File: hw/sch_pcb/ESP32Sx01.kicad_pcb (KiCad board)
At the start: 2 copper layers, 60.5 x 50.3 mm, 32 parts, among them J1 HEADER_1x03, J2 USBC_USB4105-GF-A, J3 HEADER_1x12, J4 HEADER_1x12, J5 HEADER_1x12, J6 HEADER_1x03, J7 HEADER_1x03, J8 HEADER_2x05, Q1 BC817-25, SW1 434133025816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

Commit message: Update of PCB design
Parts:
- removed J7: HEADER_1x03, Mlab_Pin_Headers:Straight_2x03
- added Y1: Crystal_Small, Mlab_XTAL:ABS07, B.Cu at (152.4, 104.7)
- SW1: moved to F.Cu
- moved C7 80.8 mm to (162.2, 87.4), turned to 90 degrees
- moved C4 73.3 mm to (154.0, 102.6)
- moved C5 69.4 mm to (150.5, 102.6), turned to 0 degrees
- moved R1 64.4 mm to (168.9, 119.6), turned to 0 degrees
- moved SW1 58.3 mm to (130.1, 92.8), turned to 90 degrees
- moved R2 58.2 mm to (160.0, 119.7)
- moved D1 42.7 mm to (166.9, 84.7), turned to -90 degrees
- moved J1 40.6 mm to (153.1, 117.2)
- moved J6 34.5 mm to (132.7, 117.2)
- moved C6 33.1 mm to (135.6, 88.1)
- moved R4 29.6 mm to (164.3, 87.4), turned to -90 degrees
- moved R6 18.4 mm to (127.7, 83.8), turned to -90 degrees
- moved R3 18.0 mm to (134.0, 86.1), turned to 0 degrees
- moved Q1 15.8 mm to (128.1, 87.8), turned to 0 degrees
- moved R5 14.2 mm to (131.8, 88.2)
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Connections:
- J4 pad 1: Net-(J4-Pad1) -> GND
- J4 pad 10: Net-(J4-Pad10) -> /GPIO17
- J4 pad 11: Net-(J4-Pad11) -> /GPIO18
- J4 pad 12: Net-(J4-Pad11) -> /GPIO18
- J4 pad 13: Net-(J4-Pad13) -> /GPIO21
- J4 pad 14: Net-(J4-Pad13) -> /GPIO21
- J4 pad 15: Net-(J4-Pad15) -> /GPIO47
- J4 pad 16: Net-(J4-Pad15) -> /GPIO47
- J4 pad 17: Net-(J4-Pad17) -> /GPIO48
- J4 pad 18: Net-(J4-Pad17) -> /GPIO48
- J4 pad 19: Net-(J4-Pad19) -> GND
- J4 pad 2: Net-(J4-Pad1) -> GND
- J4 pad 20: Net-(J4-Pad19) -> GND
- J4 pad 21: Net-(J4-Pad21) -> +3V3
- J4 pad 22: Net-(J4-Pad21) -> +3V3
- J4 pad 23: Net-(J4-Pad23) -> GND
- J4 pad 24: Net-(J4-Pad23) -> GND
- J4 pad 3: Net-(J4-Pad3) -> /GPIO12
- J4 pad 4: Net-(J4-Pad3) -> /GPIO12
- J4 pad 5: Net-(J4-Pad5) -> /GPIO13
- J4 pad 6: Net-(J4-Pad5) -> /GPIO13
- J4 pad 7: Net-(J4-Pad7) -> /GPIO14
- J4 pad 8: Net-(J4-Pad7) -> /GPIO14
- J4 pad 9: Net-(J4-Pad10) -> /GPIO17
- U3 pad 28: /GPIO33 -> unconnected-(U3-SPIIO4/GPIO33/FSPIHD/SUBSPIHD-Pad28)
- U3 pad 29: /GPIO34 -> unconnected-(U3-SPIIO5/GPIO34/FSPICS0/SUBSPICS0-Pad29)
- U3 pad 31: /GPIO35 -> unconnected-(U3-SPIIO6/GPIO35/FSPID/SUBSPID-Pad31)
- U3 pad 32: /GPIO36 -> unconnected-(U3-SPIIO7/GPIO36/FSPICLK/SUBSPICLK-Pad32)
- U3 pad 33: /GPIO37 -> unconnected-(U3-SPIDQS/GPIO37/FSPIQ/SUBSPIQ-Pad33)
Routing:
- net +3V3: track 0.00 -> 120.2 mm, vias 0 -> 3
- net /GPIO21: track 0.00 -> 49.8 mm, vias 0 -> 2
- net /GPIO12: track 0.00 -> 32.8 mm, vias 0 -> 1
- net +5V: track 0.00 -> 31.8 mm, vias 0 -> 4
- net /GPIO13: track 0.00 -> 30.2 mm, vias 0 -> 1
- net /GPIO18: track 0.00 -> 30.1 mm, vias 0 -> 1
- net /GPIO17: track 0.00 -> 29.5 mm, vias 0 -> 1
- net /GPIO14: track 0.00 -> 29.3 mm, vias 0 -> 1
- net /GPIO47: track 0.00 -> 28.6 mm, vias 0 -> 1
- net /GPIO48: track 0.00 -> 28.5 mm, vias 0 -> 1
- net /USB_DP: track 0.00 -> 21.2 mm
- net /USB_DN: track 0.00 -> 20.9 mm
- net /en: track 0.00 -> 19.2 mm, vias 0 -> 1
- net Net-(J2-D--PadA7): track 0.00 -> 9.47 mm
- net Net-(J2-D+-PadA6): track 0.00 -> 8.89 mm
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- added copper zone on B.Cu, net GND
- added copper zone on F.Cu, net GND
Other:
- outline, holes or cut-outs redrawn
- board text added: "RST"

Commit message: finishing PCB design
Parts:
- moved SW1 2.12 mm to (132.3, 92.8), turned to -90 degrees
- moved J4 0.83 mm to (142.9, 125.8)
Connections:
- J5 pad 1: /GPIO35 -> GND
- J5 pad 2: /GPIO35 -> GND
- J5 pad 3: /GPIO36 -> +3V3
- J5 pad 4: /GPIO36 -> +3V3
- J5 pad 5: /GPIO37 -> GND
- J5 pad 6: /GPIO37 -> GND
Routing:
- net /GPIO35: track 30.8 -> 0.00 mm
- net /GPIO37: track 27.8 -> 0.00 mm
- net /GPIO36: track 26.5 -> 0.00 mm
- net +3V3: track 120.2 -> 134.2 mm
- net GND: track 4.74 -> 9.75 mm, vias 37 -> 51
- net /GPIO21: track 49.8 -> 50.6 mm
- net /GPIO17: track 29.5 -> 30.3 mm
- net /GPIO48: track 28.5 -> 29.4 mm
- net /GPIO47: track 28.6 -> 29.4 mm
- net /GPIO18: track 30.1 -> 30.9 mm
- net /GPIO14: track 29.3 -> 30.1 mm
- net /GPIO11: track 33.9 -> 33.1 mm
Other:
- board text added: "- + - 48 47 21 18 17 14 13 12 -"
- board text added: "- 3v3 - G48 G47 G21 G18 G17 G14 13 12 -"
- board text added: "11 10 9 8 7 6 5 4 3 2 1 0"
- board text added: "2026"
- board text added: "46 45 44 43 42 41 40 39 38 - + -"
- board text added: "ESP32Sx01A"
- board text added: "ESP32Sx01A MLAB"
- board text added: "G0 G1 G2 G3 G4 G5 G6 G7 G8 G9 G10 G11"
- board text added: "G46 G45 G44 G43 G42 G41 G40 G39 G38 GND 3v3 GND"
- board text added: "GND 3v3 GND"
- board text added: "GND 5V(in) GND"
- board text added: "GND SDA-G8 3v3 SCL-G9 GND"
- board text added: "MLAB.cz"
- board text added: "MLAB.cz, 2026 roman-dvorak"
- board text added: "PWR"
- board text added: "USB"
- board text added: "USR"

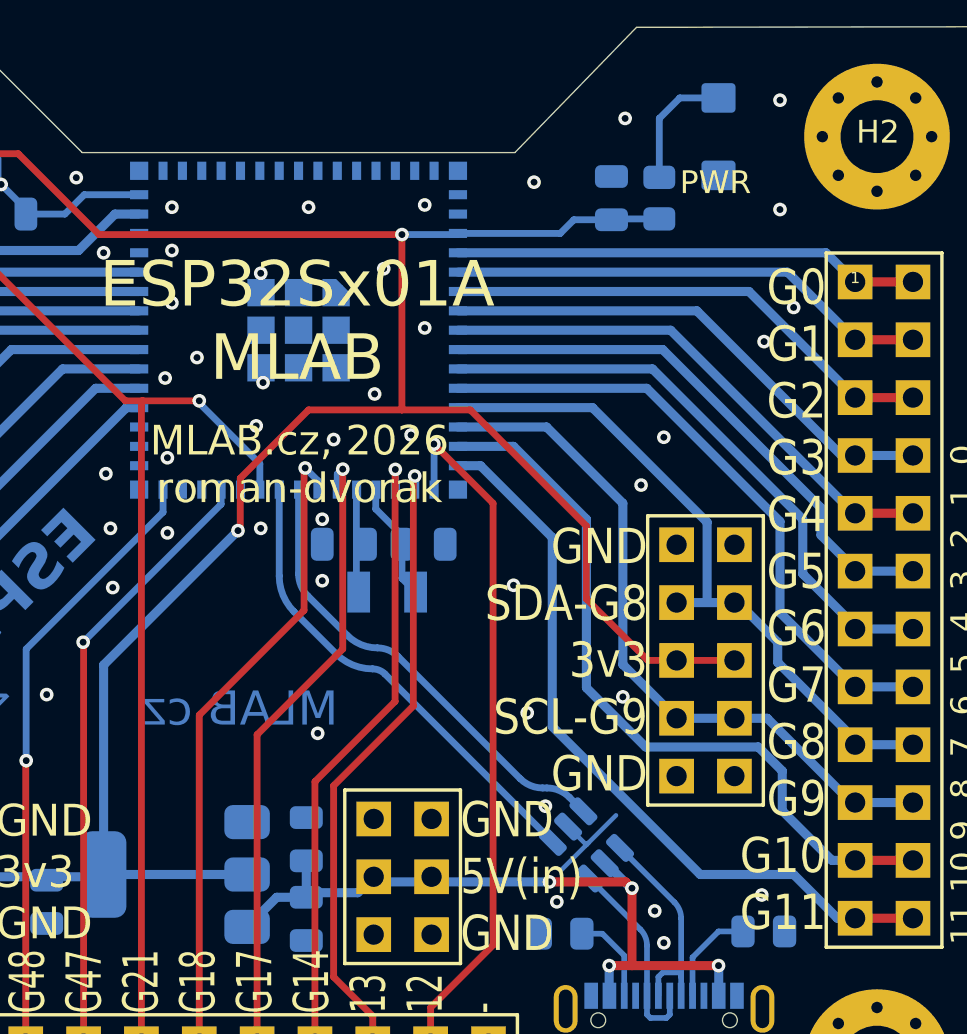
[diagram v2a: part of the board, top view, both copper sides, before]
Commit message: move boot button
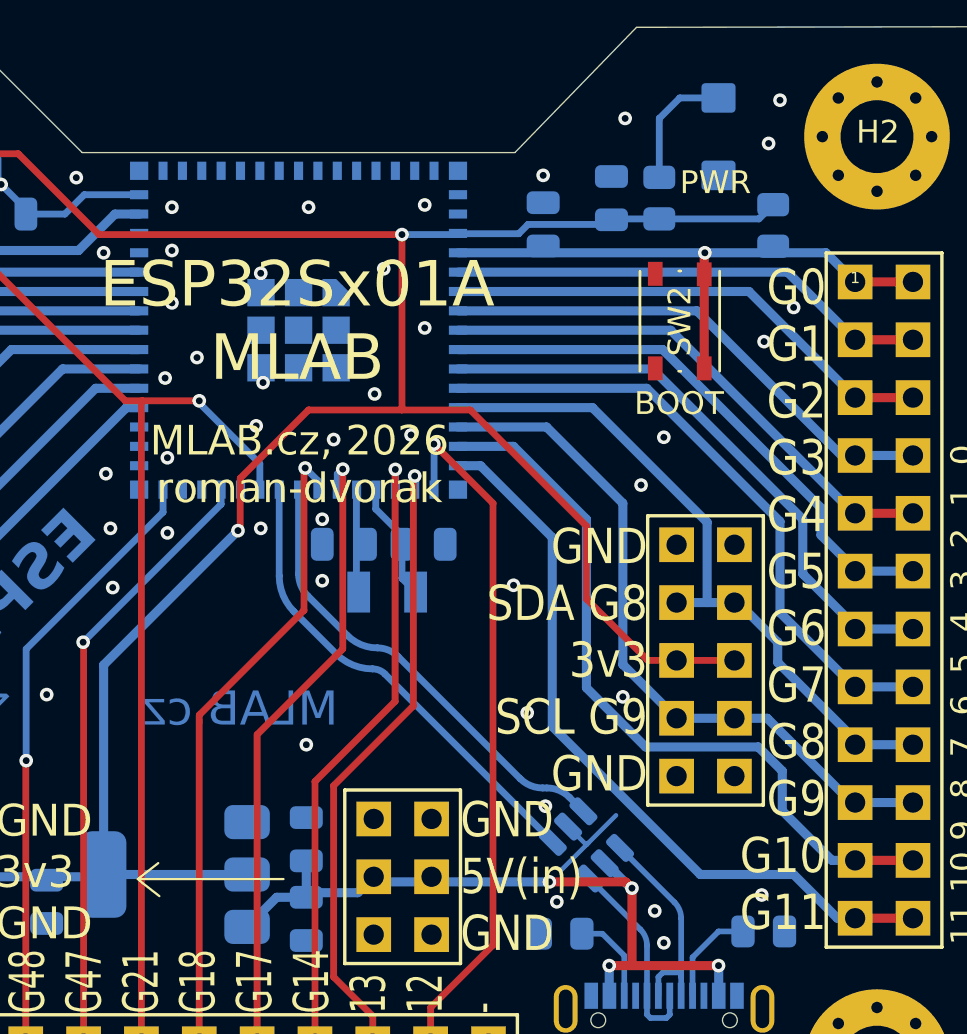
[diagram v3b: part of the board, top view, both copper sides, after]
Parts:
- added C7: 100n, Capacitor_SMD:C_0805_2012Metric, B.Cu at (159.2, 88.5)
- added R4: 1k, Resistor_SMD:R_0805_2012Metric, B.Cu at (169.3, 88.6)
- added SW2: 434133025816, Button_Switch_SMD:SW_Push_1P1T_NO_Vertical_Wuerth_434133025816, F.Cu at (165.2, 92.8)
- renumbered C7 to C8, J8 to J7, R4 to R5, R5 to R6, R6 to R7
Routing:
- net +3V3: track 134.2 -> 139.5 mm
- net /GPIO0_BOOT: track 20.5 -> 25.6 mm, vias 0 -> 1
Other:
- board text added: "BOOT"
- board text added: "GND SDA G8 3v3 SCL G9 GND"
- board text removed: "GND SDA-G8 3v3 SCL-G9 GND"

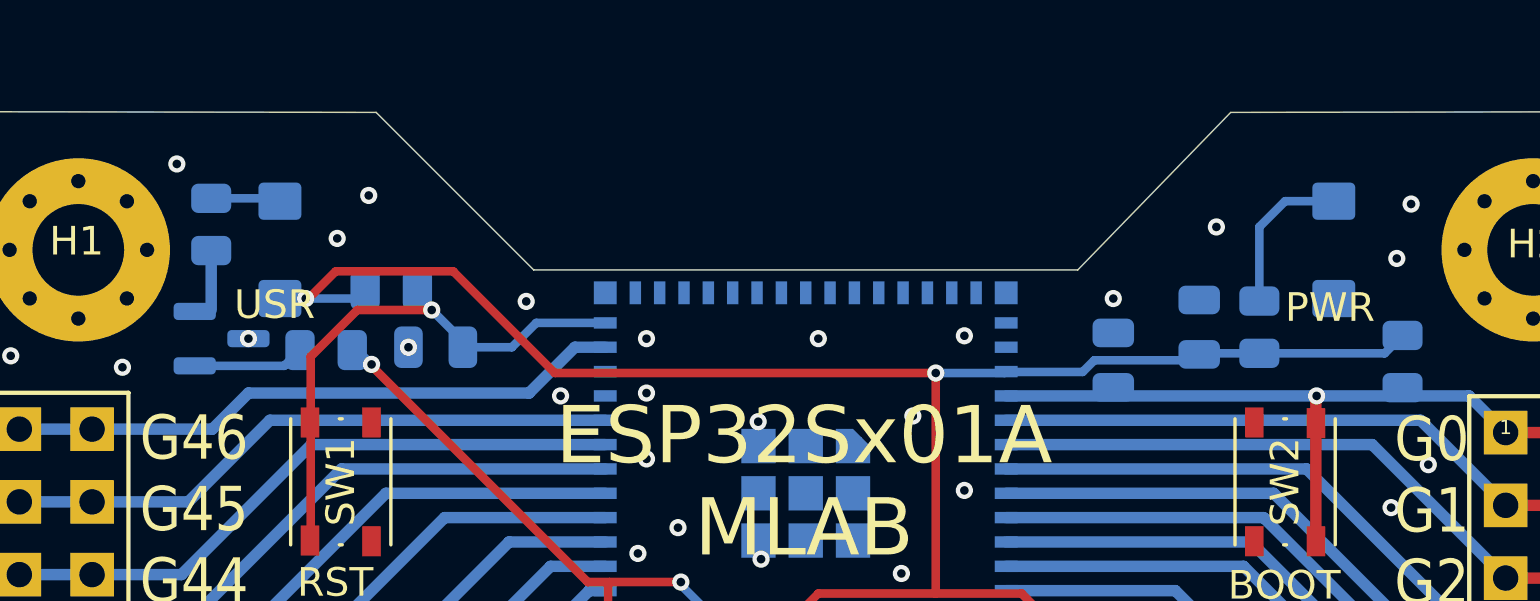
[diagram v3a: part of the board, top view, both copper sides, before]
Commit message: rotate LED to maintain same orientation
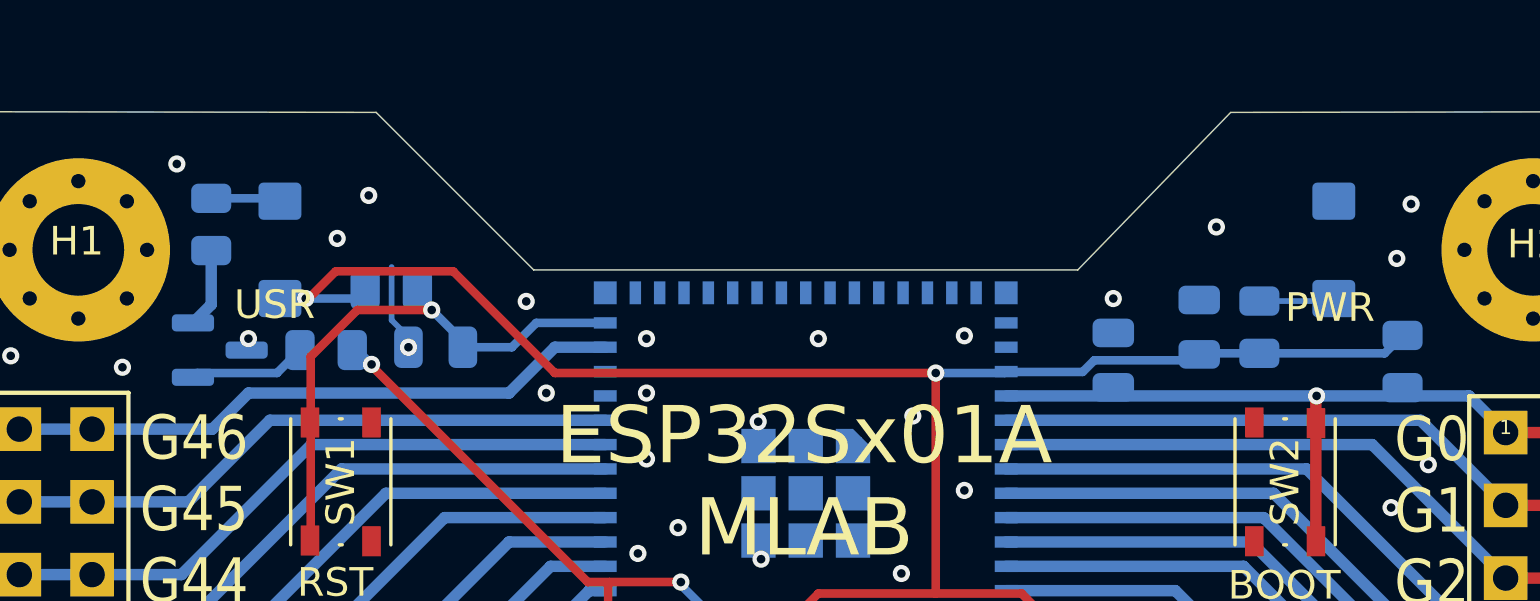
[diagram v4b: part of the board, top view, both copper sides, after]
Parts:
- moved Q1 0.40 mm to (128.0, 88.2)
- turned D1 to 90 degrees
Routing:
- net GND: track 9.75 -> 12.8 mm
- net Net-(D1-A): track 5.56 -> 2.64 mm
- net Net-(Q1-C): track 2.08 -> 2.79 mm
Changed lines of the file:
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@@
 	(footprint "Package_TO_SOT_SMD:SOT-23"
 		(layer "B.Cu")
-		(at 128.102499 87.78)
+		(at 128.04 88.18)
 		(descr "SOT, 3 Pin (JEDEC TO-236 Var AB https://www.jedec.org/document_search?search_api_views_fulltext=TO-236), generated with kicad-footprint-generator ipc_gullwing_generator.py")
 		(tags "SOT TO_SOT_SMD")
@@
 	(footprint "Mlab_D:LED_1206_KPTR"
 		(layer "B.Cu")
-		(at 166.94 84.68 -90)
+		(at 166.94 84.68 90)
 		(descr "Diode Mini-MELF Standard")
 		(tags "Diode Mini-MELF Standard")
 		(property "Reference" "D1"
-			(at 4.4 0 270)
+			(at 4.4 0 90)
 			(unlocked yes)
 			(layer "B.SilkS")
@@
 		)
 		(property "Value" "Red"
-			(at 0 -2.7 270)
+			(at 0 -2.7 90)
 			(unlocked yes)
 			(layer "B.SilkS")
@@
 		)
 		(property "Obchod" "OK"
-			(at 0 0 90)
+			(at 0 0 270)
 			(unlocked yes)
 			(layer "B.Fab")
@@
 		(attr smd)
 		(fp_line
-			(start -1.65 1.2)
-			(end 2.5 1.2)
+			(start 2.5 -1.2)
+			(end -1.65 -1.2)
 			(stroke
 				(width 0.15)
@@
 		)
 		(fp_line
-			(start 2.5 -1.2)
-			(end -1.65 -1.2)
+			(start -1.65 1.2)
+			(end 2.5 1.2)
 			(stroke
 				(width 0.15)
@@
 		)
 		(fp_line
-			(start -2.5 1.2)
-			(end 2.5 1.2)
+			(start 2.5 -1.2)
+			(end -2.5 -1.2)
 			(stroke
 				(width 0.15)
@@
 		)
 		(fp_line
-			(start 2.5 1.2)
-			(end 2.5 -1.2)
+			(start -2.5 -1.2)
+			(end -2.5 1.2)
 			(stroke
 				(width 0.15)
@@
 		)
 		(fp_line
-			(start -2.5 -1.2)
-			(end -2.5 1.2)
+			(start 2.5 1.2)
+			(end 2.5 -1.2)
 			(stroke
 				(width 0.15)
@@
 		)
 		(fp_line
-			(start 2.5 -1.2)
-			(end -2.5 -1.2)
+			(start -2.5 1.2)
+			(end 2.5 1.2)
 			(stroke
 				(width 0.15)
@@
 		)
 		(fp_text user "K"
-			(at 1.854199 -0.0508 270)
+			(at 1.854199 -0.0508 90)
 			(unlocked yes)
 			(layer "B.Fab")
@@
 		)
 		(fp_text user "K"
-			(at 2.032 -0.0508 90)
+			(at 2.032 -0.0508 270)
 			(unlocked yes)
 			(layer "F.Fab")
@@
 		)
 		(pad "" np_thru_hole oval
-			(at 0 0 270)
+			(at 0 0 90)
 			(size 1.9 2.4)
 			(drill oval 1.9 2.4)
@@
 		)
 		(pad "1" smd roundrect
-			(at 1.700001 0 90)
+			(at 1.700001 0 270)
 			(size 1.3 1.5)
 			(layers "B.Cu" "B.Mask" "B.Paste")
@@
 		)
 		(pad "2" smd roundrect
-			(at -1.700001 0 270)
+			(at -1.700001 0 90)
 			(size 1.3 1.5)
 			(layers "B.Cu" "B.Mask" "B.Paste")
@@
 	)
 	(via
-		(at 139.94 89.78)
+		(at 139.44 89.68)
 		(size 0.6)
 		(drill 0.3)
@@
 	)
 	(segment
+		(start 134.04 87.13625)
+		(end 134.04 85.28)
+		(width 0.2)
+		(layer "B.Cu")
+		(net 1)
+	)
+	(segment
 		(start 123.58 118.88)
 		(end 121.04 118.88)
@@
 	)
 	(segment
+		(start 134.6275 88.08)
+		(end 134.6275 87.72375)
+		(width 0.2)
+		(layer "B.Cu")
+		(net 1)
+	)
+	(segment
+		(start 134.6275 87.72375)
+		(end 134.04 87.13625)
+		(width 0.2)
+		(layer "B.Cu")
+		(net 1)
+	)
+	(segment
 		(start 166.94 121.08)
 		(end 163.14 121.08)
@@
 	)
 	(segment
-		(start 166.94 82.979999)
-		(end 165.240001 82.979999)
-		(width 0.3)
-		(layer "B.Cu")
-		(net 5)
-	)
-	(segment
-		(start 165.240001 82.979999)
-		(end 164.34 83.88)
-		(width 0.3)
+		(start 164.34 86.4675)
+		(end 166.852501 86.4675)
+		(width 0.2)
 		(layer "B.Cu")
 		(net 5)
 	)
 	(segment
-		(start 164.34 83.88)
-		(end 164.34 86.4675)
-		(width 0.3)
+		(start 166.852501 86.4675)
+		(end 166.94 86.380001)
+		(width 0.2)
 		(layer "B.Cu")
 		(net 5)
@@
 	(segment
 		(start 127.74 84.705)
-		(end 127.74 86.78)
+		(end 127.74 86.5925)
+		(width 0.4)
+		(layer "B.Cu")
+		(net 13)
+	)
+	(segment
+		(start 127.74 86.5925)
+		(end 127.1025 87.23)
 		(width 0.4)
 		(layer "B.Cu")
@@
 	)
 	(segment
-		(start 130.29 88.73)
+		(start 127.164999 89.067501)
+		(end 127.1025 89.13)
+		(width 0.3)
+		(layer "B.Cu")
+		(net 14)
+	)
+	(segment
+		(start 130.04 88.98)
 		(end 130.84 88.18)
 		(width 0.3)
@@
 	)
 	(segment
-		(start 127.164999 88.73)
-		(end 130.29 88.73)
+		(start 127.1025 89.13)
+		(end 127.2525 88.98)
+		(width 0.3)
+		(layer "B.Cu")
+		(net 14)
+	)
+	(segment
+		(start 127.2525 88.98)
+		(end 130.04 88.98)
 		(width 0.3)
 		(layer "B.Cu")
@@
 	)
 	(segment
-		(start 127.78 90.94)
-		(end 121.04 90.94)
+		(start 129.04 89.68)
+		(end 127.78 90.94)
 		(width 0.4)
 		(layer "B.Cu")
@@
 	)
 	(segment
-		(start 140.44 88.08)
-		(end 138.84 89.68)
+		(start 127.78 90.94)
+		(end 121.04 90.94)
 		(width 0.4)
 		(layer "B.Cu")
@@
 	)
 	(segment
-		(start 141.5 88.08)
-		(end 140.44 88.08)
+		(start 138.14 89.68)
+		(end 129.04 89.68)
 		(width 0.4)
 		(layer "B.Cu")
@@
 	)
 	(segment
-		(start 138.84 89.68)
-		(end 129.04 89.68)
+		(start 141.5 88.08)
+		(end 139.74 88.08)
 		(width 0.4)
 		(layer "B.Cu")
@@
 	)
 	(segment
-		(start 129.04 89.68)
-		(end 127.78 90.94)
+		(start 139.74 88.08)
+		(end 138.14 89.68)
 		(width 0.4)
 		(layer "B.Cu")
